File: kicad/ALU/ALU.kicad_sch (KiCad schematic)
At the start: 83 parts, among them J1 Control Connector, J2 Data Connector, U1 74LS377, U10 74LS253, U11 74LS253, U12 74LS253, U13 74LS253, U14 74LS253, U15 74LS253, U16 74LS253, U17 74F382, U18 74F382, U19 74F382, U2 74LS377, U20 74F382, U21 74F382, U22 74LS283, U23 74LS283, U24 74LS283, U25 74LS283, U26 74LS283, U27 74LS244, U28 74LS244, U29 74LS244, U3 74LS377, U30 74LS86, U31 74LS08, U32 74LS32, U33 74LS04, U34 74LS253, U35 74LS27, U36 74LS27, U37 74LS11, U38 74LS257, U39 74LS32, U4 74LS377, U5 74LS377, U6 74LS377, U7 74LS253, U8 74LS253, U9 74LS253

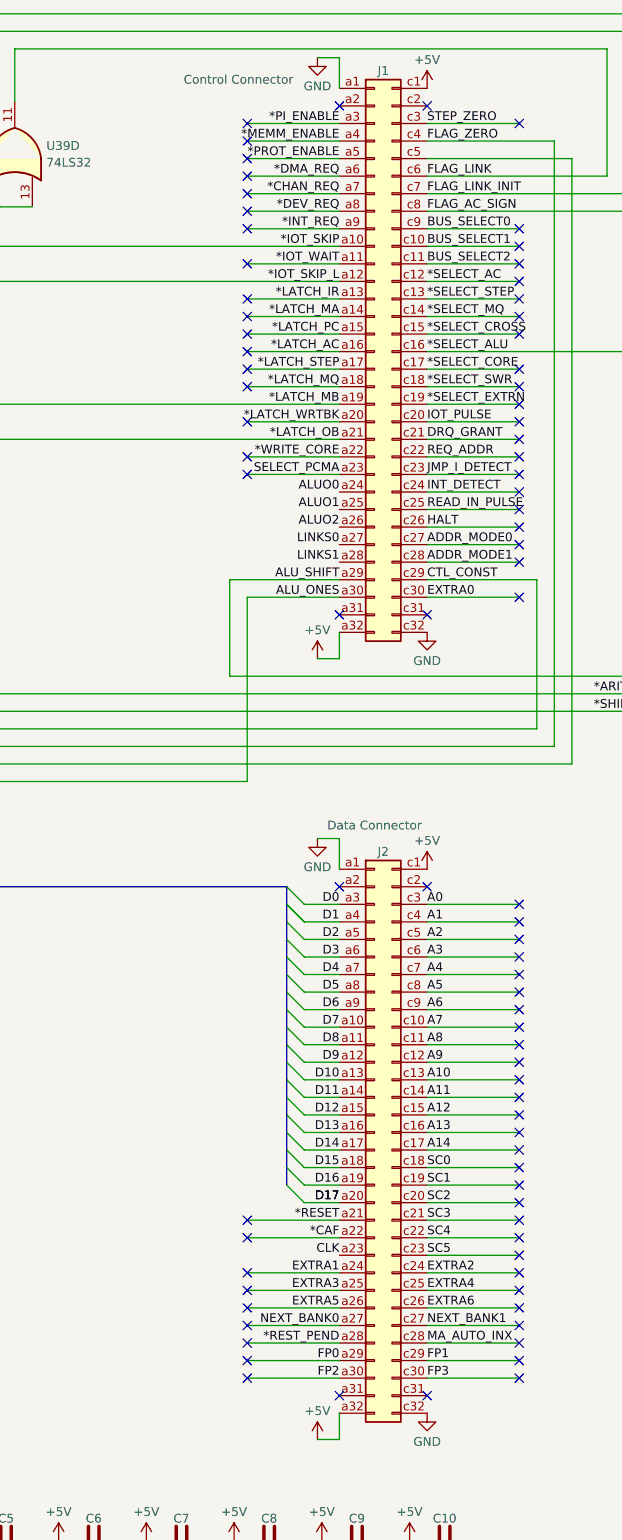
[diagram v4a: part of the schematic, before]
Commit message: Start work on backplane and fix connectors
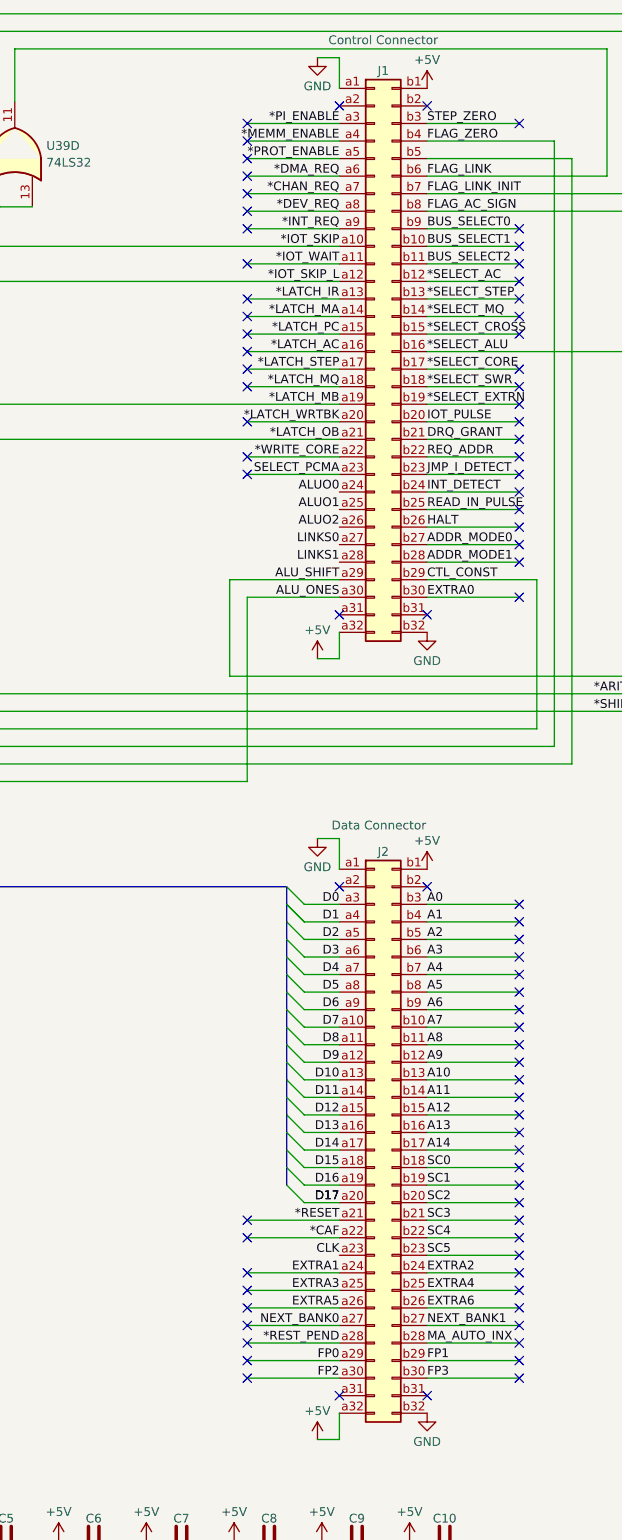
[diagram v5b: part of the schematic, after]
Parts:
- removed J1: Control Connector, Connector_DIN:DIN41612_B_2x32_Male_Horizontal_THT, symbol Connector:DIN41612_02x32_AC
- removed J2: Data Connector, Connector_DIN:DIN41612_B_2x32_Male_Horizontal_THT, symbol Connector:DIN41612_02x32_AC
- added J1: Control Connector, Connector_DIN:DIN41612_B_2x32_Male_Horizontal_THT, symbol Connector:DIN41612_02x32_AB
- added J2: Data Connector, Connector_DIN:DIN41612_B_2x32_Male_Horizontal_THT, symbol Connector:DIN41612_02x32_AB
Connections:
- net *CAF: now also J2.a22 (Pin_a22)
- net *CHAN_REQ: now also J1.a7 (Pin_a7)
- net *DEV_REQ: now also J1.a8 (Pin_a8)
- net *DMA_REQ: now also J1.a6 (Pin_a6)
- net *INT_REQ: now also J1.a9 (Pin_a9)
- net *IOT_SKIP: now also J1.a10 (Pin_a10)
- net *IOT_SKIP_L: now also J1.a12 (Pin_a12)
- net *IOT_WAIT: now also J1.a11 (Pin_a11)
- net *LATCH_AC: now also J1.a16 (Pin_a16)
- net *LATCH_IR: now also J1.a13 (Pin_a13)
- net *LATCH_MA: now also J1.a14 (Pin_a14)
- net *LATCH_MB: now also J1.a19 (Pin_a19)
- net *LATCH_MQ: now also J1.a18 (Pin_a18)
- net *LATCH_OB: now also J1.a21 (Pin_a21)
- net *LATCH_PC: now also J1.a15 (Pin_a15)
- net *LATCH_STEP: now also J1.a17 (Pin_a17)
- net *LATCH_WRTBK: now also J1.a20 (Pin_a20)
- net *MEMM_ENABLE: now also J1.a4 (Pin_a4)
- net *PI_ENABLE: now also J1.a3 (Pin_a3)
- net *PROT_ENABLE: now also J1.a5 (Pin_a5)
- net *RESET: now also J2.a21 (Pin_a21)
- net *REST_PEND: now also J2.a28 (Pin_a28)
- net *SELECT_AC: now also J1.b12 (Pin_b12)
- net *SELECT_ALU: now also J1.b16 (Pin_b16)
- net *SELECT_CORE: now also J1.b17 (Pin_b17)
- net *SELECT_CROSS: now also J1.b15 (Pin_b15)
- net *SELECT_EXTRN: now also J1.b19 (Pin_b19)
- net *SELECT_MQ: now also J1.b14 (Pin_b14)
- net *SELECT_STEP: now also J1.b13 (Pin_b13)
- net *SELECT_SWR: now also J1.b18 (Pin_b18)
- net *WRITE_CORE: now also J1.a22 (Pin_a22)
- net +5V: now also J1.a32 (Pin_a32), J1.b1 (Pin_b1), J2.a32 (Pin_a32), J2.b1 (Pin_b1)
- net A0: now also J2.b3 (Pin_b3)
- net A1: now also J2.b4 (Pin_b4)
- net A10: now also J2.b13 (Pin_b13)
- net A11: now also J2.b14 (Pin_b14)
- net A12: now also J2.b15 (Pin_b15)
- net A13: now also J2.b16 (Pin_b16)
- net A14: now also J2.b17 (Pin_b17)
- net A2: now also J2.b5 (Pin_b5)
- net A3: now also J2.b6 (Pin_b6)
- net A4: now also J2.b7 (Pin_b7)
- net A5: now also J2.b8 (Pin_b8)
- net A6: now also J2.b9 (Pin_b9)
- net A7: now also J2.b10 (Pin_b10)
- net A8: now also J2.b11 (Pin_b11)
- net A9: now also J2.b12 (Pin_b12)
- net ADDR_MODE0: now also J1.b27 (Pin_b27)
- net ADDR_MODE1: now also J1.b28 (Pin_b28)
- net ALUO0: now also J1.a24 (Pin_a24)
- net ALUO1: now also J1.a25 (Pin_a25)
- net ALUO2: now also J1.a26 (Pin_a26)
- net ALU_ONES: now also J1.a30 (Pin_a30)
- net ALU_SHIFT: now also J1.a29 (Pin_a29)
- net BUS_SELECT0: now also J1.b9 (Pin_b9)
- net BUS_SELECT1: now also J1.b10 (Pin_b10)
- net BUS_SELECT2: now also J1.b11 (Pin_b11)
- net CLK: now also J2.a23 (Pin_a23)
- net CTL_CONST: now also J1.b29 (Pin_b29)
- net D0: now also J2.a3 (Pin_a3)
- net D1: now also J2.a4 (Pin_a4)
- net D10: now also J2.a13 (Pin_a13)
- net D11: now also J2.a14 (Pin_a14)
- net D12: now also J2.a15 (Pin_a15)
- net D13: now also J2.a16 (Pin_a16)
- net D14: now also J2.a17 (Pin_a17)
- net D15: now also J2.a18 (Pin_a18)
- net D16: now also J2.a19 (Pin_a19)
- net D17: now also J2.a20 (Pin_a20)
- net D2: now also J2.a5 (Pin_a5)
- net D3: now also J2.a6 (Pin_a6)
- net D4: now also J2.a7 (Pin_a7)
- net D5: now also J2.a8 (Pin_a8)
- net D6: now also J2.a9 (Pin_a9)
- net D7: now also J2.a10 (Pin_a10)
- net D8: now also J2.a11 (Pin_a11)
- net D9: now also J2.a12 (Pin_a12)
- net DRQ_GRANT: now also J1.b21 (Pin_b21)
- net EXTRA0: now also J1.b30 (Pin_b30)
- net EXTRA1: now also J2.a24 (Pin_a24)
- net EXTRA2: now also J2.b24 (Pin_b24)
- net EXTRA3: now also J2.a25 (Pin_a25)
- net EXTRA4: now also J2.b25 (Pin_b25)
- net EXTRA5: now also J2.a26 (Pin_a26)
- net EXTRA6: now also J2.b26 (Pin_b26)
- net FLAG_AC_SIGN: now also J1.b8 (Pin_b8)
- net FLAG_LINK: now also J1.b6 (Pin_b6)
- net FLAG_LINK_INIT: now also J1.b7 (Pin_b7)
- net FLAG_ZERO: now also J1.b4 (Pin_b4)
- net FP0: now also J2.a29 (Pin_a29)
- net FP1: now also J2.b29 (Pin_b29)
- net FP2: now also J2.a30 (Pin_a30)
- net FP3: now also J2.b30 (Pin_b30)
- net GND: now also J1.a1 (Pin_a1), J1.b32 (Pin_b32), J2.a1 (Pin_a1), J2.b32 (Pin_b32)
- net HALT: now also J1.b26 (Pin_b26)
- net INT_DETECT: now also J1.b24 (Pin_b24)
- net IOT_PULSE: now also J1.b20 (Pin_b20)
- net JMP_I_DETECT: now also J1.b23 (Pin_b23)
- net LINKS0: now also J1.a27 (Pin_a27)
- net LINKS1: now also J1.a28 (Pin_a28)
- net MA_AUTO_INX: now also J2.b28 (Pin_b28)
- net NEXT_BANK0: now also J2.a27 (Pin_a27)
- net NEXT_BANK1: now also J2.b27 (Pin_b27)
- net OB17: now also J1.b5 (Pin_b5)
- net READ_IN_PULSE: now also J1.b25 (Pin_b25)
- net REQ_ADDR: now also J1.b22 (Pin_b22)
- net SC0: now also J2.b18 (Pin_b18)
- net SC1: now also J2.b19 (Pin_b19)
- net SC2: now also J2.b20 (Pin_b20)
- net SC3: now also J2.b21 (Pin_b21)
- net SC4: now also J2.b22 (Pin_b22)
- net SC5: now also J2.b23 (Pin_b23)
- net SELECT_PCMA: now also J1.a23 (Pin_a23)
- net STEP_ZERO: now also J1.b3 (Pin_b3)
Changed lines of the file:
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@@
     )
   )
-  (symbol (lib_id "Connector:DIN41612_02x32_AC") (at 506.095 175.26 0) (unit 1)
-    (in_bom yes) (on_board yes) (dnp no)
-    (property "Reference" "J2" (at 507.365 134.62 0)
-      (effects (font (size 1.27 1.27)))
-    )
-    (property "Value" "Data Connector" (at 506.095 130.81 0)
-      (effects (font (size 1.27 1.27)))
-    )
-    (property "Footprint" "Connector_DIN:DIN41612_B_2x32_Male_Horizontal_THT" (at 506.095 175.26 0)
-      (effects (font (size 1.27 1.27)) hide)
-    )
-    (property "Datasheet" "~" (at 506.095 175.26 0)
-      (effects (font (size 1.27 1.27)) hide)
-    )
-    (pin "a1")
-    (pin "a10")
-    (pin "a11")
-    (pin "a12")
-    (pin "a13")
-    (pin "a14")
-    (pin "a15")
-    (pin "a16")
-    (pin "a17")
-    (pin "a18")
-    (pin "a19")
-    (pin "a2")
-    (pin "a20")
-    (pin "a21")
-    (pin "a22")
-    (pin "a23")
-    (pin "a24")
-    (pin "a25")
-    (pin "a26")
-    (pin "a27")
-    (pin "a28")
-    (pin "a29")
-    (pin "a3")
-    (pin "a30")
-    (pin "a31")
-    (pin "a32")
-    (pin "a4")
-    (pin "a5")
-    (pin "a6")
-    (pin "a7")
-    (pin "a8")
-    (pin "a9")
-    (pin "c1")
-    (pin "c10")
-    (pin "c11")
-    (pin "c12")
-    (pin "c13")
-    (pin "c14")
-    (pin "c15")
-    (pin "c16")
-    (pin "c17")
-    (pin "c18")
-    (pin "c19")
-    (pin "c2")
-    (pin "c20")
-    (pin "c21")
-    (pin "c22")
-    (pin "c23")
-    (pin "c24")
-    (pin "c25")
-    (pin "c26")
-    (pin "c27")
-    (pin "c28")
-    (pin "c29")
-    (pin "c3")
-    (pin "c30")
-    (pin "c31")
-    (pin "c32")
-    (pin "c4")
-    (pin "c5")
-    (pin "c6")
-    (pin "c7")
-    (pin "c8")
-    (pin "c9")
-    (instances
-      (project "ALU"
-        (path "/b26dce39-0c19-4808-8ddd-74847f21ad13"
-          (reference "J2") (unit 1)
-        )
-      )
-    )
-  )
   (symbol (lib_id "power:+5V") (at 363.22 115.57 0) (unit 1)
     (in_bom yes) (on_board yes) (dnp no) (fields_autoplaced)
@@
     )
   )
+  (symbol (lib_id "Connector:DIN41612_02x32_AB") (at 506.095 62.23 0) (unit 1)
+    (in_bom yes) (on_board yes) (dnp no)
+    (property "Reference" "J1" (at 507.365 21.59 0)
+      (effects (font (size 1.27 1.27)))
+    )
+    (property "Value" "Control Connector" (at 507.365 17.145 0)
+      (effects (font (size 1.27 1.27)))
+    )
+    (property "Footprint" "Connector_DIN:DIN41612_B_2x32_Male_Horizontal_THT" (at 506.095 62.23 0)
+      (effects (font (size 1.27 1.27)) hide)
+    )
+    (property "Datasheet" "~" (at 506.095 62.23 0)
+      (effects (font (size 1.27 1.27)) hide)
+    )
+    (pin "a1")
+    (pin "a10")
+    (pin "a11")
+    (pin "a12")
+    (pin "a13")
+    (pin "a14")
+    (pin "a15")
+    (pin "a16")
+    (pin "a17")
+    (pin "a18")
+    (pin "a19")
+    (pin "a2")
+    (pin "a20")
+    (pin "a21")
+    (pin "a22")
+    (pin "a23")
+    (pin "a24")
+    (pin "a25")
+    (pin "a26")
+    (pin "a27")
+    (pin "a28")
+    (pin "a29")
+    (pin "a3")
+    (pin "a30")
+    (pin "a31")
+    (pin "a32")
+    (pin "a4")
+    (pin "a5")
+    (pin "a6")
+    (pin "a7")
+    (pin "a8")
+    (pin "a9")
+    (pin "b1")
+    (pin "b10")
+    (pin "b11")
+    (pin "b12")
+    (pin "b13")
+    (pin "b14")
+    (pin "b15")
+    (pin "b16")
+    (pin "b17")
+    (pin "b18")
+    (pin "b19")
+    (pin "b2")
+    (pin "b20")
+    (pin "b21")
+    (pin "b22")
+    (pin "b23")
+    (pin "b24")
+    (pin "b25")
+    (pin "b26")
+    (pin "b27")
+    (pin "b28")
+    (pin "b29")
+    (pin "b3")
+    (pin "b30")
+    (pin "b31")
+    (pin "b32")
+    (pin "b4")
+    (pin "b5")
+    (pin "b6")
+    (pin "b7")
+    (pin "b8")
+    (pin "b9")
+    (instances
+      (project "ALU"
+        (path "/b26dce39-0c19-4808-8ddd-74847f21ad13"
+          (reference "J1") (unit 1)
+        )
+      )
+    )
+  )
   (symbol (lib_id "power:+5V") (at 396.875 247.65 0) (unit 1)
     (in_bom yes) (on_board yes) (dnp no) (fields_autoplaced)
@@
     )
   )
+  (symbol (lib_id "Connector:DIN41612_02x32_AB") (at 506.095 175.26 0) (unit 1)
+    (in_bom yes) (on_board yes) (dnp no)
+    (property "Reference" "J2" (at 507.365 134.62 0)
+      (effects (font (size 1.27 1.27)))
+    )
+    (property "Value" "Data Connector" (at 506.73 130.81 0)
+      (effects (font (size 1.27 1.27)))
+    )
+    (property "Footprint" "Connector_DIN:DIN41612_B_2x32_Male_Horizontal_THT" (at 506.095 175.26 0)
+      (effects (font (size 1.27 1.27)) hide)
+    )
+    (property "Datasheet" "~" (at 506.095 175.26 0)
+      (effects (font (size 1.27 1.27)) hide)
+    )
+    (pin "a1")
+    (pin "a10")
+    (pin "a11")
+    (pin "a12")
+    (pin "a13")
+    (pin "a14")
+    (pin "a15")
+    (pin "a16")
+    (pin "a17")
+    (pin "a18")
+    (pin "a19")
+    (pin "a2")
+    (pin "a20")
+    (pin "a21")
+    (pin "a22")
+    (pin "a23")
+    (pin "a24")
+    (pin "a25")
+    (pin "a26")
+    (pin "a27")
+    (pin "a28")
+    (pin "a29")
+    (pin "a3")
+    (pin "a30")
+    (pin "a31")
+    (pin "a32")
+    (pin "a4")
+    (pin "a5")
+    (pin "a6")
+    (pin "a7")
+    (pin "a8")
+    (pin "a9")
+    (pin "b1")
+    (pin "b10")
+    (pin "b11")
+    (pin "b12")
+    (pin "b13")
+    (pin "b14")
+    (pin "b15")
+    (pin "b16")
+    (pin "b17")
+    (pin "b18")
+    (pin "b19")
+    (pin "b2")
+    (pin "b20")
+    (pin "b21")
+    (pin "b22")
+    (pin "b23")
+    (pin "b24")
+    (pin "b25")
+    (pin "b26")
+    (pin "b27")
+    (pin "b28")
+    (pin "b29")
+    (pin "b3")
+    (pin "b30")
+    (pin "b31")
+    (pin "b32")
+    (pin "b4")
+    (pin "b5")
+    (pin "b6")
+    (pin "b7")
+    (pin "b8")
+    (pin "b9")
+    (instances
+      (project "ALU"
+        (path "/b26dce39-0c19-4808-8ddd-74847f21ad13"
+          (reference "J2") (unit 1)
+        )
+      )
+    )
+  )
   (symbol (lib_id "power:GND") (at 483.235 272.415 0) (unit 1)
     (in_bom yes) (on_board yes) (dnp no) (fields_autoplaced)
@@
         )
       )
-    )
-  )
-  (symbol (lib_id "Connector:DIN41612_02x32_AC") (at 506.095 62.23 0) (unit 1)
-    (in_bom yes) (on_board yes) (dnp no)
-    (property "Reference" "J1" (at 507.365 21.59 0)
-      (effects (font (size 1.27 1.27)))
-    )
-    (property "Value" "Control Connector" (at 486.41 22.86 0)
-      (effects (font (size 1.27 1.27)))
-    )
-    (property "Footprint" "Connector_DIN:DIN41612_B_2x32_Male_Horizontal_THT" (at 506.095 62.23 0)
-      (effects (font (size 1.27 1.27)) hide)
-    )
-    (property "Datasheet" "~" (at 506.095 62.23 0)
-      (effects (font (size 1.27 1.27)) hide)
-    )
-    (pin "a1")
-    (pin "a10")
-    (pin "a11")
-    (pin "a12")
-    (pin "a13")
-    (pin "a14")
-    (pin "a15")
-    (pin "a16")
-    (pin "a17")
-    (pin "a18")
-    (pin "a19")
-    (pin "a2")
-    (pin "a20")
-    (pin "a21")
-    (pin "a22")
-    (pin "a23")
-    (pin "a24")
-    (pin "a25")
-    (pin "a26")
-    (pin "a27")
-    (pin "a28")
-    (pin "a29")
-    (pin "a3")
-    (pin "a30")
-    (pin "a31")
-    (pin "a32")
-    (pin "a4")
-    (pin "a5")
-    (pin "a6")
-    (pin "a7")
-    (pin "a8")
-    (pin "a9")
-    (pin "c1")
-    (pin "c10")
-    (pin "c11")
-    (pin "c12")
-    (pin "c13")
-    (pin "c14")
-    (pin "c15")
-    (pin "c16")
-    (pin "c17")
-    (pin "c18")
-    (pin "c19")
-    (pin "c2")
-    (pin "c20")
-    (pin "c21")
-    (pin "c22")
-    (pin "c23")
-    (pin "c24")
-    (pin "c25")
-    (pin "c26")
-    (pin "c27")
-    (pin "c28")
-    (pin "c29")
-    (pin "c3")
-    (pin "c30")
-    (pin "c31")
-    (pin "c32")
-    (pin "c4")
-    (pin "c5")
-    (pin "c6")
-    (pin "c7")
-    (pin "c8")
-    (pin "c9")
-    (instances
-      (project "ALU"
-        (path "/b26dce39-0c19-4808-8ddd-74847f21ad13"
-          (reference "J1") (unit 1)
-        )
-      )

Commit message: Update backplane pin logic levels
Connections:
- net DRQ_GRANT renamed *DRQ_GRANT
- net INT_DETECT renamed *INT_DETECT
- net IOT_PULSE renamed *IOT_PULSE
- net JMP_I_DETECT renamed *JMP_I_DETECT
- net READ_IN_PULSE renamed *READ_IN_PULSE
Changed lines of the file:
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@@
     (effects (font (size 1.27 1.27)) (justify left bottom))
   )
-  (label "IOT_PULSE" (at 513.715 72.39 0) (fields_autoplaced)
+  (label "*IOT_PULSE" (at 513.715 72.39 0) (fields_autoplaced)
     (effects (font (size 1.27 1.27)) (justify left bottom))
   )
@@
     (effects (font (size 1.27 1.27)) (justify left bottom))
   )
-  (label "INT_DETECT" (at 513.715 82.55 0) (fields_autoplaced)
+  (label "*INT_DETECT" (at 513.715 82.55 0) (fields_autoplaced)
     (effects (font (size 1.27 1.27)) (justify left bottom))
   )
@@
     (effects (font (size 1.27 1.27)) (justify left bottom))
   )
-  (label "JMP_I_DETECT" (at 513.715 80.01 0) (fields_autoplaced)
+  (label "*JMP_I_DETECT" (at 513.715 80.01 0) (fields_autoplaced)
     (effects (font (size 1.27 1.27)) (justify left bottom))
   )
@@
     (effects (font (size 1.27 1.27)) (justify left bottom))
   )
-  (label "READ_IN_PULSE" (at 513.715 85.09 0) (fields_autoplaced)
+  (label "*READ_IN_PULSE" (at 513.715 85.09 0) (fields_autoplaced)
     (effects (font (size 1.27 1.27)) (justify left bottom))
   )
@@
     (effects (font (size 1.27 1.27)) (justify right bottom))
   )
-  (label "DRQ_GRANT" (at 513.715 74.93 0) (fields_autoplaced)
-    (effects (font (size 1.27 1.27)) (justify left bottom))
-  )
+  (label "*DRQ_GRANT" (at 513.715 74.93 0) (fields_autoplaced)
+    (effects (font (size 1.27 1.27)) (justify left bottom))
+  )
